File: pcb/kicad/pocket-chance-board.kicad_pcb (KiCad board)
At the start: 4 copper layers, 150 x 100 mm, 150 parts, among them J1 SWD, J2 USB4085-GF-A, J3 LiPo JST-PH 2.0mm (1 = + RED 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, J4 LCD 1.54in ST7789 module, JST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, J5 Speaker JST-PH, J6 microSD Molex 104031-0811, J7 STEMMA QT, J8 Expansion (6 = VBAT_SENSE ADC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, J9 LCD header 2.54 mm (wire by n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, Q1 FS8205A, Q3 AO3400A, Q4 AO3401A, Q6 AO3401A (DNP: fit only for a 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, SW1 BOOT, SW10 DPAD LEFT PTS645SM43SMTR92, SW11 DPAD RIGHT PTS645SM43SMTR92, SW12 DPAD PRESS PTS645SM43SMTR92, SW2 RESET, SW3 POWER PCM12, SW4 A PTS125SM43SMTR2LFS, SW5 B PTS125SM43SMTR2LFS, SW6 X PTS125SM43SMTR2LFS, SW7 Y PTS125SM43SMTR2LFS, SW8 DPAD UP PTS645SM43SMTR92, SW9 DPAD DOWN PTS645SM43SMTR92, U1 RP2350A, U10 LSM6DSOXTR, U11 RM2, U2 W25Q128JVSIQ, U3 APS6404L-3SQR-SN, U4 USBLC6-2SC6, U5 BQ24074RGTR, U6 TPS63001DRCR, U7 DW01A, U8 PAM8302AADCR, U9 DS3231MZ+, Y1 12MHz ABM8-272-T3

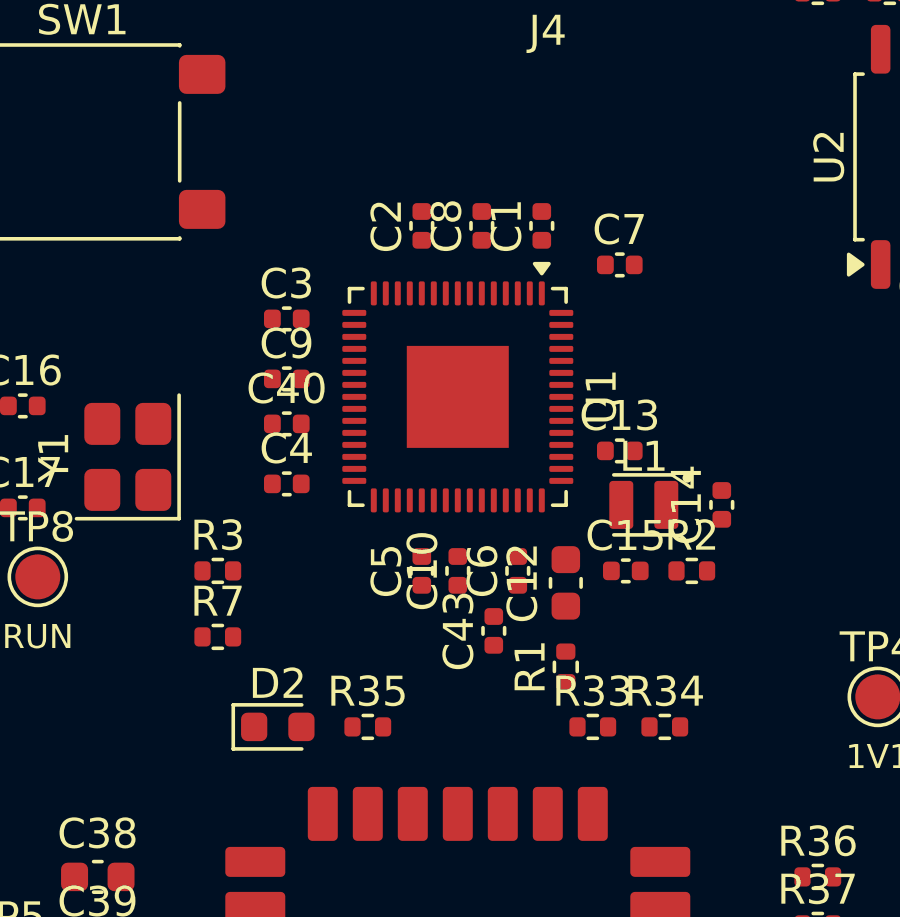
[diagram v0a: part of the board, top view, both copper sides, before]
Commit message: Routing stage 1: RP2350 decoupling escapes (locked), cap ground vias, 3x3 exposed-pad vias; caps face their pins; C43 at pin 44
- gen_pcb: bottom-row caps re-spaced, C43 1.7 mm from ADC pin 44 with C12 behind it (auditor 20:38)
- route_critical.py stage 1, route_prep.py and ses_import.py (Freerouting pipeline) added
- STAGE2: routing method recorded (Freerouting as a standing assist, each run its own commit)
DRC: no errors besides the unrouted connections. Schematic unchanged (rev 0.11).
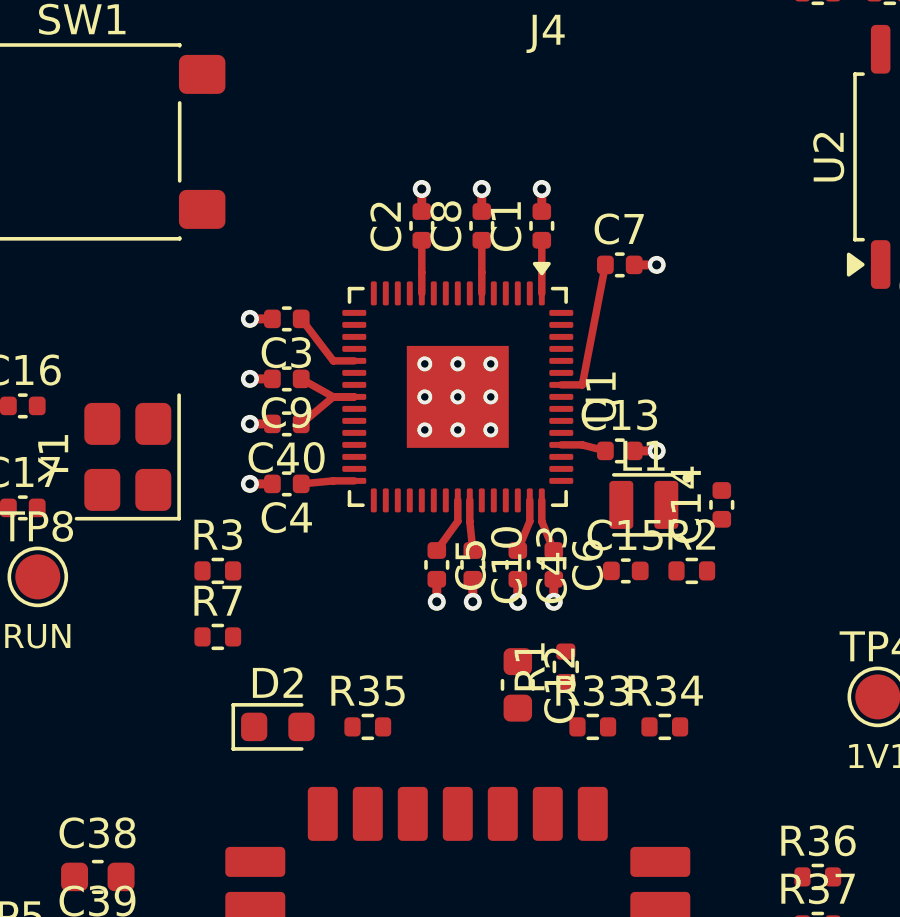
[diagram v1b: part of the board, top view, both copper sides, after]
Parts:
- moved C12 3.76 mm to (124.0, 129.6), turned to -90 degrees
- moved C43 2.34 mm to (124.0, 125.6), turned to -90 degrees
- moved C6 1.22 mm to (125.2, 125.6), turned to -90 degrees
- moved C10 0.54 mm to (122.5, 125.6), turned to -90 degrees
- moved C5 0.54 mm to (121.3, 125.6), turned to -90 degrees
- turned C3 to 180 degrees
- turned C4 to 180 degrees
- turned C40 to 180 degrees
- turned C9 to 180 degrees
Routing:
- net +3V3: track 0.00 -> 17.7 mm
- net GND: track 0.00 -> 9.75 mm, vias 0 -> 22
- net 1V1: track 0.00 -> 7.47 mm
- net ADC_AVDD: track 0.00 -> 1.75 mm

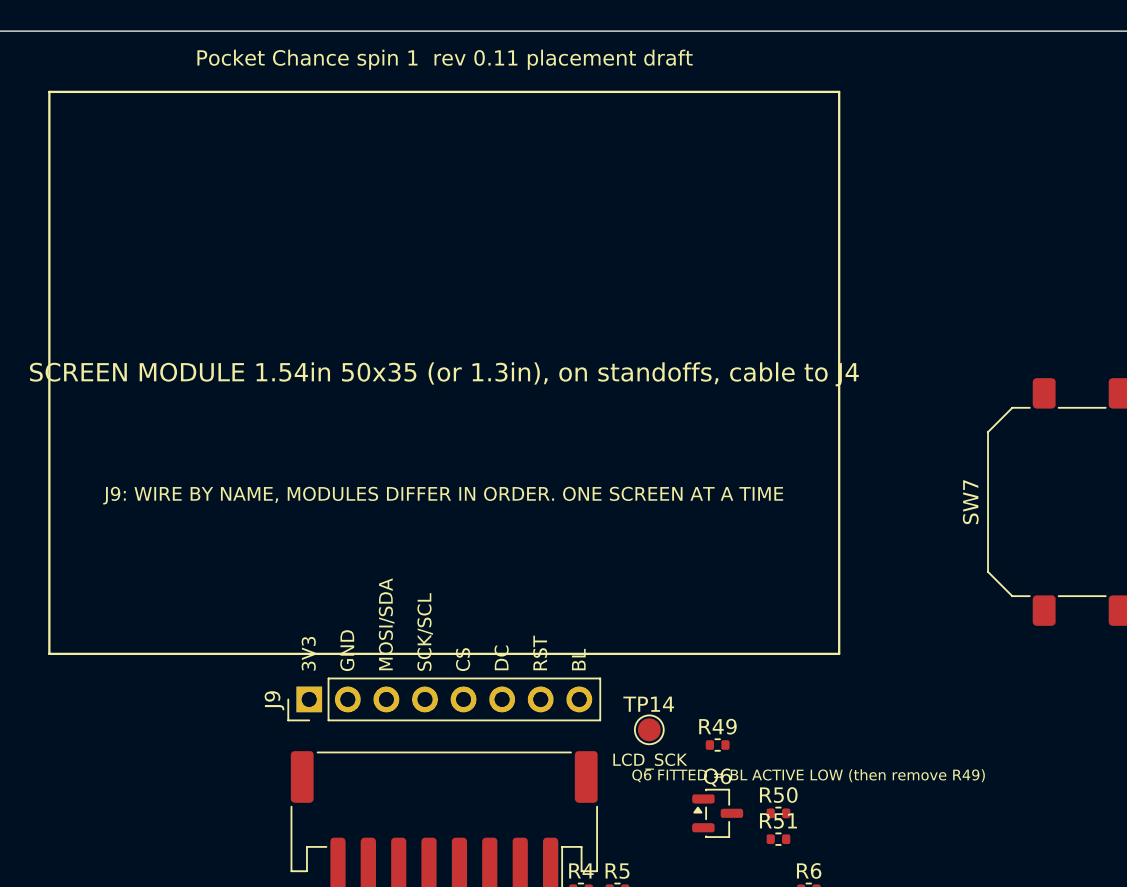
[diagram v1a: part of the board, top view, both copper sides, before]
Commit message: Rev 0.12 (John's yes): R51 2.7k / R50 100R for the unfitted backlight switch, J9 in the AITRIP pin order, stronger R49 silk
Netlist diff vs rev 0.11 (5aee6a5): R50 1k -> 100R, R51 100k -> 2.7k, J9 pins remapped (GND, 3V3, SCK,
MOSI, RST, DC, CS, BL); nothing added or removed. ERC 0 errors, 2 expected warnings. Board regenerated
with stage-1 routing; DRC only unrouted connections.
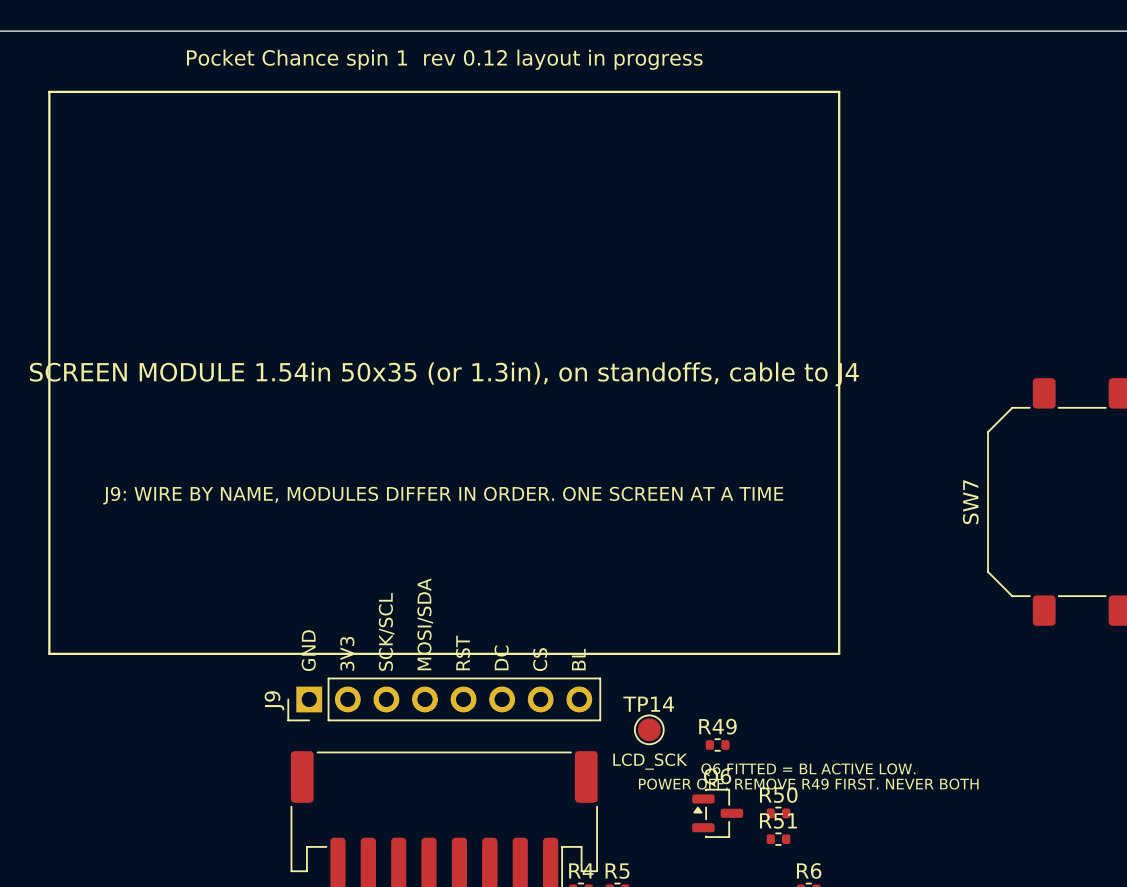
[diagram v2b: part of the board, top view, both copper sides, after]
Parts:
- R50: value 1k -> 100R
- R51: value 100k -> 2.7k
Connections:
- J9 pad 1: +3V3 -> GND
- J9 pad 2: GND -> +3V3
- J9 pad 3: LCD_MOSI -> LCD_SCK
- J9 pad 4: LCD_SCK -> LCD_MOSI
- J9 pad 5: LCD_CS -> LCD_RST
- J9 pad 7: LCD_RST -> LCD_CS
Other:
- board text added: "POWER OFF, REMOVE R49 FIRST. NEVER BOTH"
- board text added: "Pocket Chance spin 1 rev 0.12 layout in progress"
- board text added: "Q6 FITTED = BL ACTIVE LOW."
- board text removed: "Pocket Chance spin 1 rev 0.11 placement draft"
- board text removed: "Q6 FITTED = BL ACTIVE LOW (then remove R49)"
